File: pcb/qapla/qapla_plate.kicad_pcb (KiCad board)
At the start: 2 copper layers, 154.4 x 126.1 mm, 5 parts

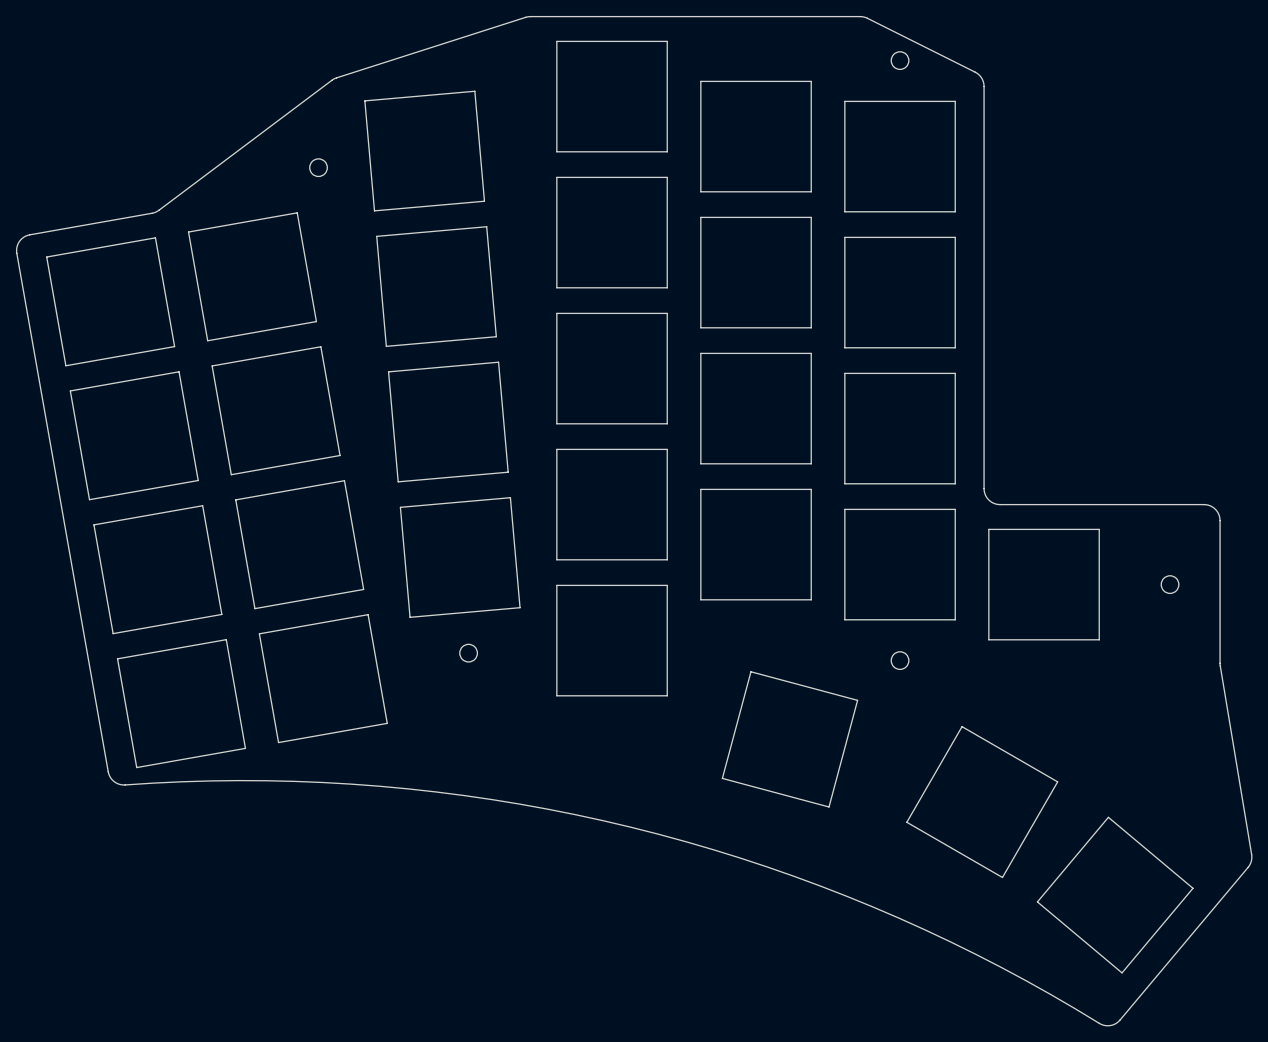
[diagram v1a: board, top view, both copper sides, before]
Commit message: Adjusting hole positions
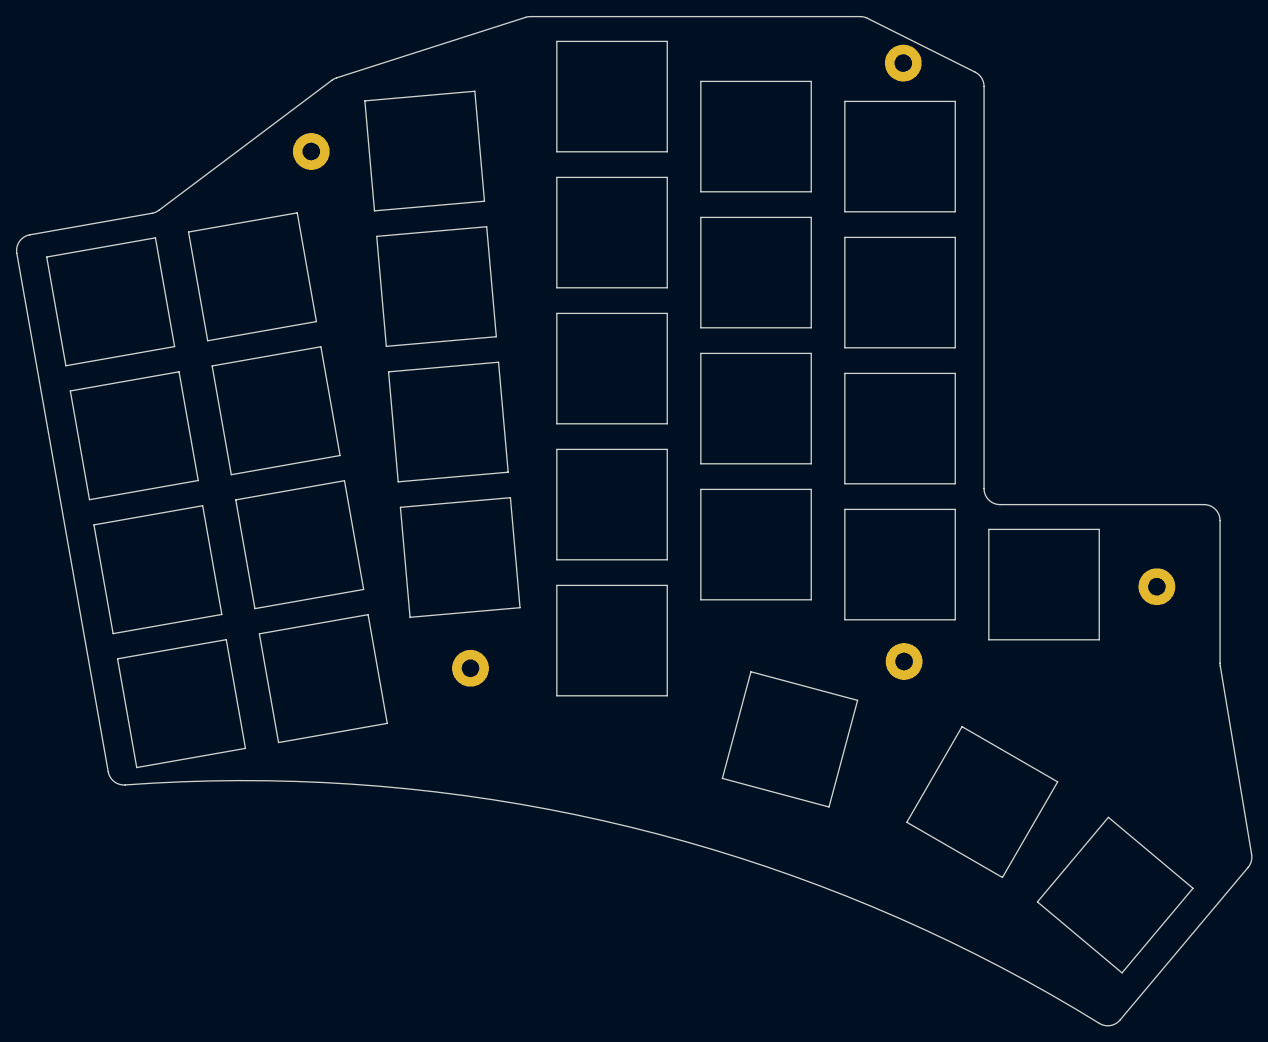
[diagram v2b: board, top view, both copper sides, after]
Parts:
- removed MH1, MH2, MH3, MH4, MH5: , ceoloide:mounting_hole_npth
- added H1: , ceoloide:mounting_hole_plated, F.Cu at (137.8, 44.6)
- added H2: , ceoloide:mounting_hole_plated, F.Cu at (157.7, 109.2)
- added H3: , ceoloide:mounting_hole_plated, F.Cu at (211.8, 33.5)
- added H4: , ceoloide:mounting_hole_plated, F.Cu at (211.9, 108.3)
- added H5: , ceoloide:mounting_hole_plated, F.Cu at (243.5, 99.0)

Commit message: Starting work on bottom case
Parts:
- moved H3 4.58 mm to (207.3, 32.7)
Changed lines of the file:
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@@
   (footprint "ceoloide:mounting_hole_plated"
     (layer "F.Cu")
-    (at 211.8 33.55 0)
+    (at 207.3 32.7 0)
     (property "Reference" "H3"
       (at 0 3 0)
